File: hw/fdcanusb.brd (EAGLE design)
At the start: 45 x 32 mm, 37 parts, among them J1 MF-CON-MICROUSB-RIGHT, J3 JST-ZH6SMT_VERT, M1 MOUNT, M2 MOUNT, M3 MOUNT, M4 MOUNT, U1 MF-REG-SOT235-3.3V-300mA, U2 USBLC6-2SC6, U3 TCAN334GSOT23, U4 TLP3317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

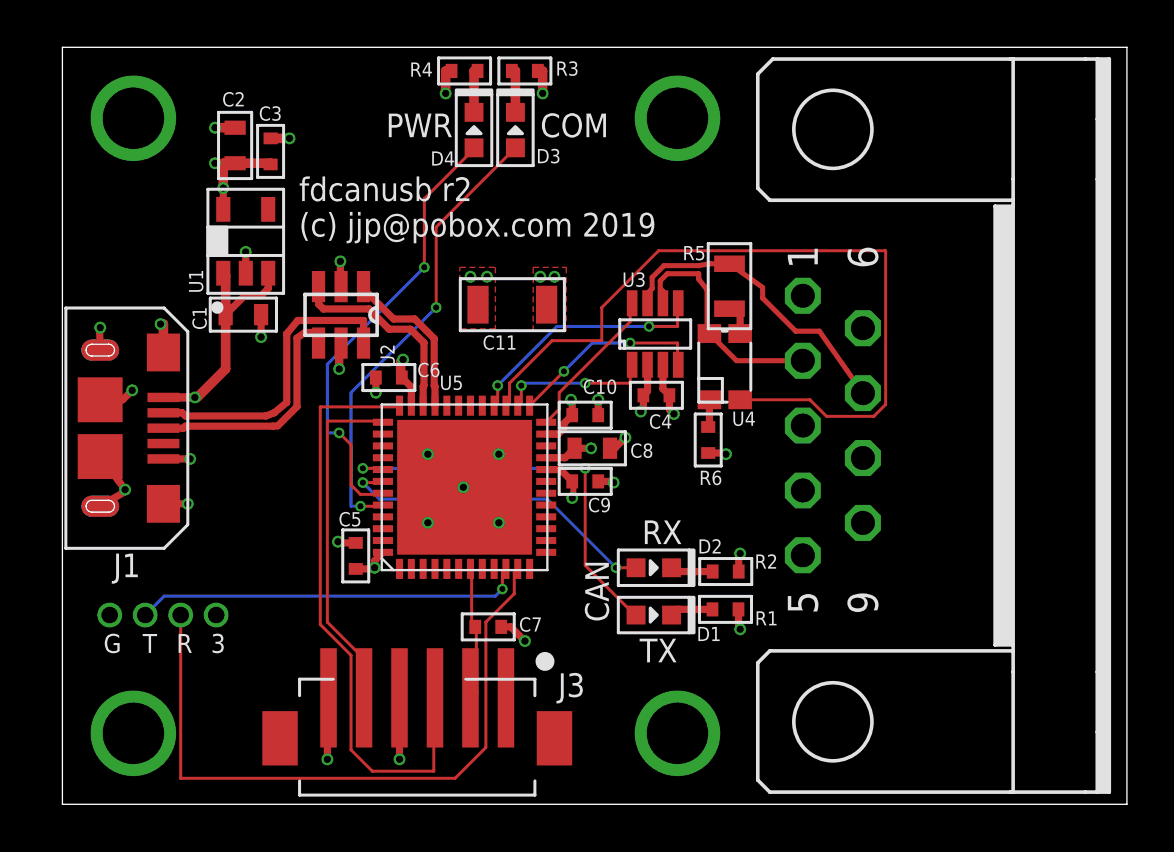
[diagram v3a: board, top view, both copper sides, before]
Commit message: Fix DB9 pinout
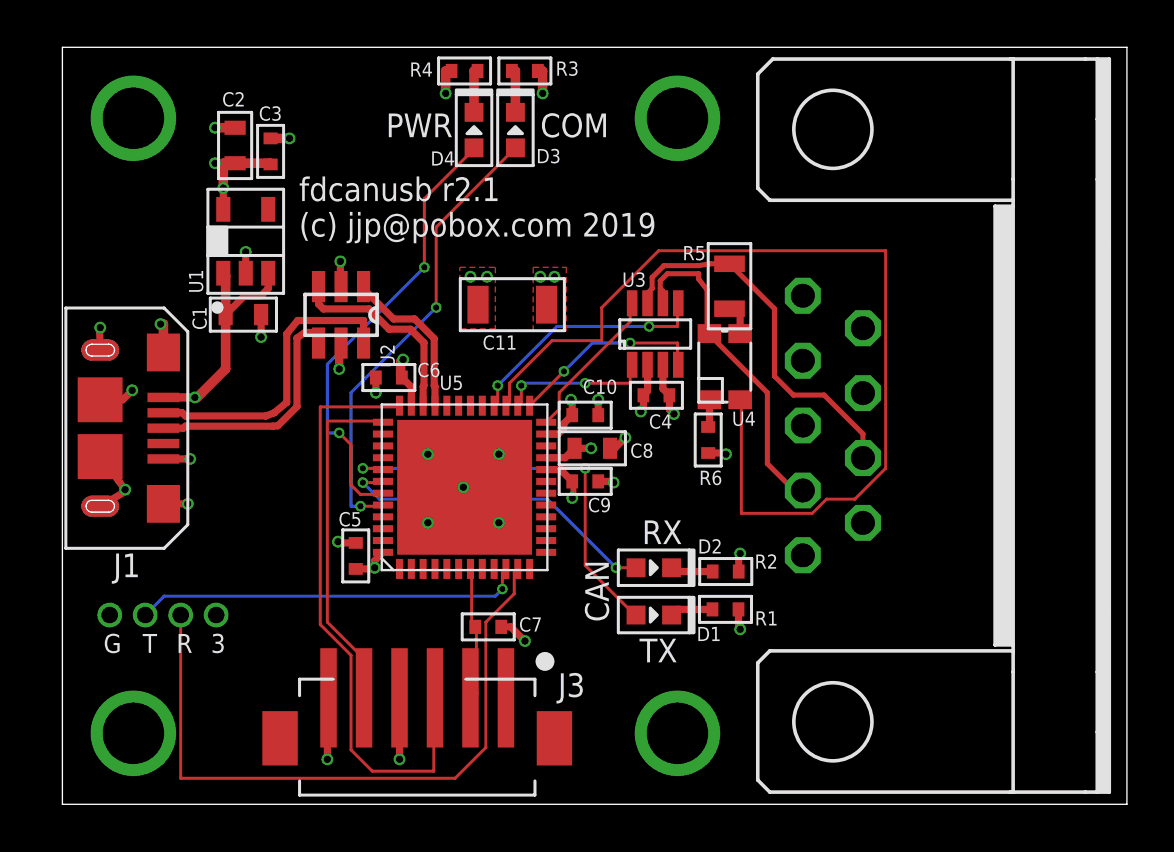
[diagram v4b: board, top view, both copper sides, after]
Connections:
- net CAN_N: now also J2.4; no longer J2.2
- net CAN_P: now also J2.8; no longer J2.7
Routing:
- net CAN_TERM: track 33.2 -> 41.0 mm
- net CAN_N: track 9.92 -> 14.0 mm
- net CAN_P: track 13.0 -> 16.0 mm
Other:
- board text added: "fdcanusb r2.1 (c) jjp@pobox.com 2019"
- board text removed: "fdcanusb r2 (c) jjp@pobox.com 2019"
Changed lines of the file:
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@@
 <wire x1="45" y1="32" x2="0" y2="32" width="0" layer="20"/>
 <wire x1="0" y1="32" x2="0" y2="0" width="0" layer="20"/>
-<text x="10" y="24" size="1" layer="21">fdcanusb r2
+<text x="10" y="24" size="1" layer="21">fdcanusb r2.1
 (c) jjp@pobox.com 2019</text>
 <text x="2.5" y="7.2" size="0.8" layer="21" rot="R180">G</text>
@@
 </signal>
 <signal name="CAN_N" class="2">
-<contactref element="J2" pad="2"/>
 <contactref element="U3" pad="6"/>
 <contactref element="U4" pad="4"/>
-<wire x1="31.3" y1="18.7532" x2="28.4968" y2="18.7532" width="0.2159" layer="1"/>
-<wire x1="28.4968" y1="18.7532" x2="27.35" y2="19.9" width="0.2159" layer="1"/>
 <wire x1="27.35" y1="19.9" x2="27.25" y2="19.9" width="0.2159" layer="1"/>
 <wire x1="27.25" y1="19.9" x2="27.25" y2="21.75" width="0.2159" layer="1"/>
@@
 <wire x1="25.27145" y1="21.8" x2="25.385" y2="21.68645" width="0.2159" layer="1"/>
 <wire x1="25.385" y1="21.68645" x2="25.385" y2="21.18" width="0.2159" layer="1"/>
+<contactref element="J2" pad="4"/>
+<wire x1="27.35" y1="19.9" x2="27.35" y2="19.85" width="0.2159" layer="1"/>
+<wire x1="27.35" y1="19.85" x2="29.8" y2="17.4" width="0.2159" layer="1"/>
+<wire x1="29.8" y1="17.4" x2="29.8" y2="14.4" width="0.2159" layer="1"/>
+<wire x1="29.8" y1="14.4" x2="30.9332" y2="13.2668" width="0.2159" layer="1"/>
+<wire x1="30.9332" y1="13.2668" x2="31.3" y2="13.2668" width="0.2159" layer="1"/>
 </signal>
 <signal name="CAN_P" class="2">
-<contactref element="J2" pad="7"/>
 <contactref element="U3" pad="7"/>
 <contactref element="R5" pad="P$1"/>
-<wire x1="33.84" y1="17.3816" x2="32" y2="20" width="0.2159" layer="1"/>
-<wire x1="32" y1="20" x2="31" y2="20" width="0.2159" layer="1"/>
-<wire x1="31" y1="20" x2="29.6" y2="21.4" width="0.2159" layer="1"/>
-<wire x1="29.6" y1="21.4" x2="29.6" y2="21.85" width="0.2159" layer="1"/>
-<wire x1="29.6" y1="21.85" x2="28.2" y2="22.85" width="0.2159" layer="1"/>
 <wire x1="28.2" y1="22.85" x2="27.37855" y2="22.85" width="0.2159" layer="1"/>
 <wire x1="27.37855" y1="22.85" x2="26.9" y2="22.77145" width="0.2159" layer="1"/>
@@
 <wire x1="24.92855" y1="21.8" x2="24.735" y2="21.60645" width="0.2159" layer="1"/>
 <wire x1="24.735" y1="21.60645" x2="24.735" y2="21.18" width="0.2159" layer="1"/>
+<contactref element="J2" pad="8"/>
+<wire x1="28.2" y1="22.85" x2="30.1" y2="20.95" width="0.2159" layer="1"/>
+<wire x1="30.1" y1="20.95" x2="30.1" y2="18.1" width="0.2159" layer="1"/>
+<wire x1="30.1" y1="18.1" x2="30.9" y2="17.3" width="0.2159" layer="1"/>
+<wire x1="30.9" y1="17.3" x2="32.2" y2="17.3" width="0.2159" layer="1"/>
+<wire x1="32.2" y1="17.3" x2="33.84" y2="15.66" width="0.2159" layer="1"/>
+<wire x1="33.84" y1="15.66" x2="33.84" y2="14.6384" width="0.2159" layer="1"/>
 </signal>
 <signal name="N$3">
@@
 <wire x1="25.2" y1="23.4" x2="22.8" y2="21" width="0.127" layer="1"/>
 <wire x1="34.8" y1="23.4" x2="25.2" y2="23.4" width="0.127" layer="1"/>
-<wire x1="34.8" y1="16.9" x2="34.8" y2="23.4" width="0.127" layer="1"/>
-<wire x1="34.3" y1="16.4" x2="34.8" y2="16.9" width="0.127" layer="1"/>
-<wire x1="32.3" y1="16.4" x2="34.3" y2="16.4" width="0.127" layer="1"/>
-<wire x1="31.6" y1="17.1" x2="32.3" y2="16.4" width="0.127" layer="1"/>
-<wire x1="28.65" y1="17.1" x2="31.6" y2="17.1" width="0.127" layer="1"/>
+<wire x1="34.8" y1="14.2" x2="34.8" y2="23.4" width="0.127" layer="1"/>
+<wire x1="33.5" y1="12.9" x2="34.8" y2="14.2" width="0.127" layer="1"/>
+<wire x1="32.3" y1="12.9" x2="33.5" y2="12.9" width="0.127" layer="1"/>
+<wire x1="31.7" y1="12.3" x2="32.3" y2="12.9" width="0.127" layer="1"/>
+<wire x1="28.7" y1="12.3" x2="31.7" y2="12.3" width="0.127" layer="1"/>
+<wire x1="28.7" y1="17.1" x2="28.7" y2="12.3" width="0.127" layer="1"/>
+<wire x1="28.7" y1="17.1" x2="28.65" y2="17.1" width="0.127" layer="1"/>
 </signal>
 <signal name="N$8">

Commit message: Update to r2.2
This just reduces the size of the PCB so it doesn't hang out so far
under the DB-9 connector.
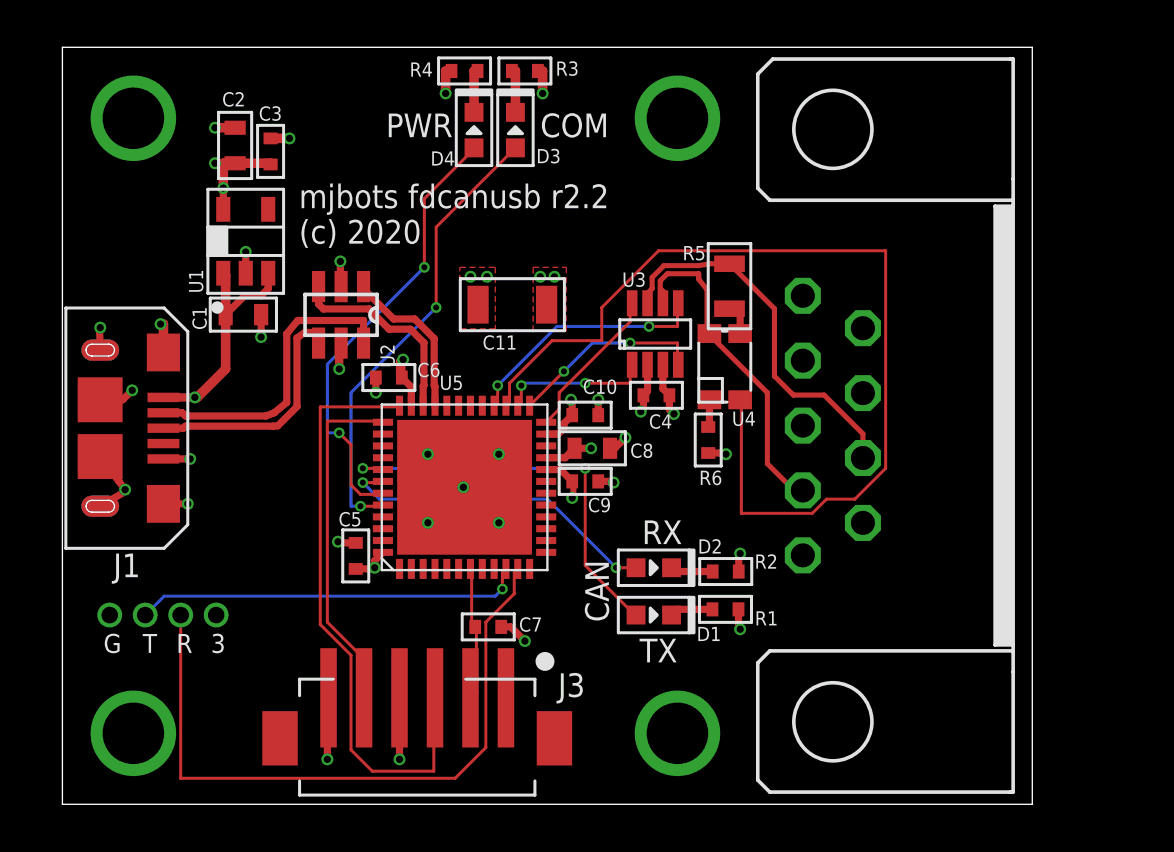
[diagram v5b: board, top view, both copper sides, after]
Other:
- board size 45 x 32 mm -> 41 x 32 mm
- board text added: "mjbots fdcanusb r2.2 (c) 2020"
- board text removed: "fdcanusb r2.1 (c) jjp@pobox.com 2019"
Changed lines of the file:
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@@
 <board>
 <plain>
-<wire x1="0" y1="0" x2="45" y2="0" width="0" layer="20"/>
-<wire x1="45" y1="0" x2="45" y2="32" width="0" layer="20"/>
-<wire x1="45" y1="32" x2="0" y2="32" width="0" layer="20"/>
+<wire x1="0" y1="0" x2="41" y2="0" width="0" layer="20"/>
+<wire x1="41" y1="0" x2="41" y2="32" width="0" layer="20"/>
+<wire x1="41" y1="32" x2="0" y2="32" width="0" layer="20"/>
 <wire x1="0" y1="32" x2="0" y2="0" width="0" layer="20"/>
-<text x="10" y="24" size="1" layer="21">fdcanusb r2.1
-(c) jjp@pobox.com 2019</text>
+<text x="10" y="23.7" size="1" layer="21">mjbots fdcanusb r2.2
+(c) 2020</text>
 <text x="2.5" y="7.2" size="0.8" layer="21" rot="R180">G</text>
 <text x="6.9" y="7.2" size="0.8" layer="21" rot="R180">3</text>
@@
 <polygon width="0.254" layer="2" thermals="no">
 <vertex x="0.5" y="31.5"/>
-<vertex x="44.5" y="31.5"/>
-<vertex x="44.5" y="0.5"/>
+<vertex x="40.5" y="31.5"/>
+<vertex x="40.5" y="0.5"/>
 <vertex x="0.5" y="0.5"/>
 </polygon>
@@
 <polygon width="0.254" layer="15" thermals="no">
 <vertex x="0.5" y="31.5"/>
-<vertex x="44.5" y="31.5"/>
-<vertex x="44.5" y="0.5"/>
+<vertex x="40.5" y="31.5"/>
+<vertex x="40.5" y="0.5"/>
 <vertex x="0.5" y="0.5"/>
 </polygon>

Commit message: Switch LED resistors back to 220s
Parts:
- R1, R2, R3, R4: value 560 -> 220
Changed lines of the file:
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@@
 <attribute name="NAME" x="16.6" y="27.6" size="0.6" layer="25" font="vector" ratio="10" rot="R180"/>
 </element>
-<element name="R1" library="mfpassives" package="R0402" value="560" x="28.03" y="8.24" smashed="yes" rot="R180">
+<element name="R1" library="mfpassives" package="R0402" value="220" x="28.03" y="8.24" smashed="yes" rot="R180">
 <attribute name="HOUSEPART" value="" x="-21.5" y="69.2" size="1.778" layer="27" rot="R180" display="off"/>
 <attribute name="TOLERANCE" value="" x="-21.5" y="69.2" size="1.778" layer="27" rot="R180" display="off"/>
-<attribute name="MPN" value="MF-RES-0402-560" x="-21.5" y="69.2" size="1.778" layer="27" rot="R180" display="off"/>
+<attribute name="MPN" value="MF-RES-0402-220" x="-21.5" y="69.2" size="1.778" layer="27" rot="R180" display="off"/>
 <attribute name="POPULATE" value="1" x="-21.5" y="69.2" size="1.778" layer="27" rot="R180" display="off"/>
 <attribute name="VOLTAGE" value="" x="-21.5" y="69.2" size="1.778" layer="27" rot="R180" display="off"/>
@@
 <attribute name="NAME" x="29.27" y="7.56" size="0.6" layer="25" font="vector" ratio="10"/>
 </element>
-<element name="R2" library="mfpassives" package="R0402" value="560" x="28.04" y="9.84" smashed="yes" rot="R180">
+<element name="R2" library="mfpassives" package="R0402" value="220" x="28.04" y="9.84" smashed="yes" rot="R180">
 <attribute name="HOUSEPART" value="" x="-25.3" y="70.8" size="1.778" layer="27" rot="R180" display="off"/>
 <attribute name="TOLERANCE" value="" x="-25.3" y="70.8" size="1.778" layer="27" rot="R180" display="off"/>
-<attribute name="MPN" value="MF-RES-0402-560" x="-25.3" y="70.8" size="1.778" layer="27" rot="R180" display="off"/>
+<attribute name="MPN" value="MF-RES-0402-220" x="-25.3" y="70.8" size="1.778" layer="27" rot="R180" display="off"/>
 <attribute name="POPULATE" value="1" x="-25.3" y="70.8" size="1.778" layer="27" rot="R180" display="off"/>
 <attribute name="VOLTAGE" value="" x="-25.3" y="70.8" size="1.778" layer="27" rot="R180" display="off"/>
@@
 <attribute name="NAME" x="29.26" y="9.96" size="0.6" layer="25" font="vector" ratio="10"/>
 </element>
-<element name="R3" library="mfpassives" package="R0402" value="560" x="19.55" y="31" smashed="yes" rot="R180">
+<element name="R3" library="mfpassives" package="R0402" value="220" x="19.55" y="31" smashed="yes" rot="R180">
 <attribute name="HOUSEPART" value="" x="5.58" y="95.77" size="1.778" layer="27" rot="R180" display="off"/>
 <attribute name="TOLERANCE" value="" x="5.58" y="95.77" size="1.778" layer="27" rot="R180" display="off"/>
-<attribute name="MPN" value="MF-RES-0402-560" x="5.58" y="95.77" size="1.778" layer="27" rot="R180" display="off"/>
+<attribute name="MPN" value="MF-RES-0402-220" x="5.58" y="95.77" size="1.778" layer="27" rot="R180" display="off"/>
 <attribute name="POPULATE" value="1" x="5.58" y="95.77" size="1.778" layer="27" rot="R180" display="off"/>
 <attribute name="VOLTAGE" value="" x="5.58" y="95.77" size="1.778" layer="27" rot="R180" display="off"/>
@@
 <attribute name="NAME" x="20.85" y="30.8" size="0.6" layer="25" font="vector" ratio="10"/>
 </element>
-<element name="R4" library="mfpassives" package="R0402" value="560" x="17" y="31" smashed="yes">
+<element name="R4" library="mfpassives" package="R0402" value="220" x="17" y="31" smashed="yes">
 <attribute name="HOUSEPART" value="" x="34.78" y="-33.77" size="1.778" layer="27" display="off"/>
 <attribute name="TOLERANCE" value="" x="34.78" y="-33.77" size="1.778" layer="27" display="off"/>
-<attribute name="MPN" value="MF-RES-0402-560" x="34.78" y="-33.77" size="1.778" layer="27" display="off"/>
+<attribute name="MPN" value="MF-RES-0402-220" x="34.78" y="-33.77" size="1.778" layer="27" display="off"/>
 <attribute name="POPULATE" value="1" x="34.78" y="-33.77" size="1.778" layer="27" display="off"/>
 <attribute name="VOLTAGE" value="" x="34.78" y="-33.77" size="1.778" layer="27" display="off"/>

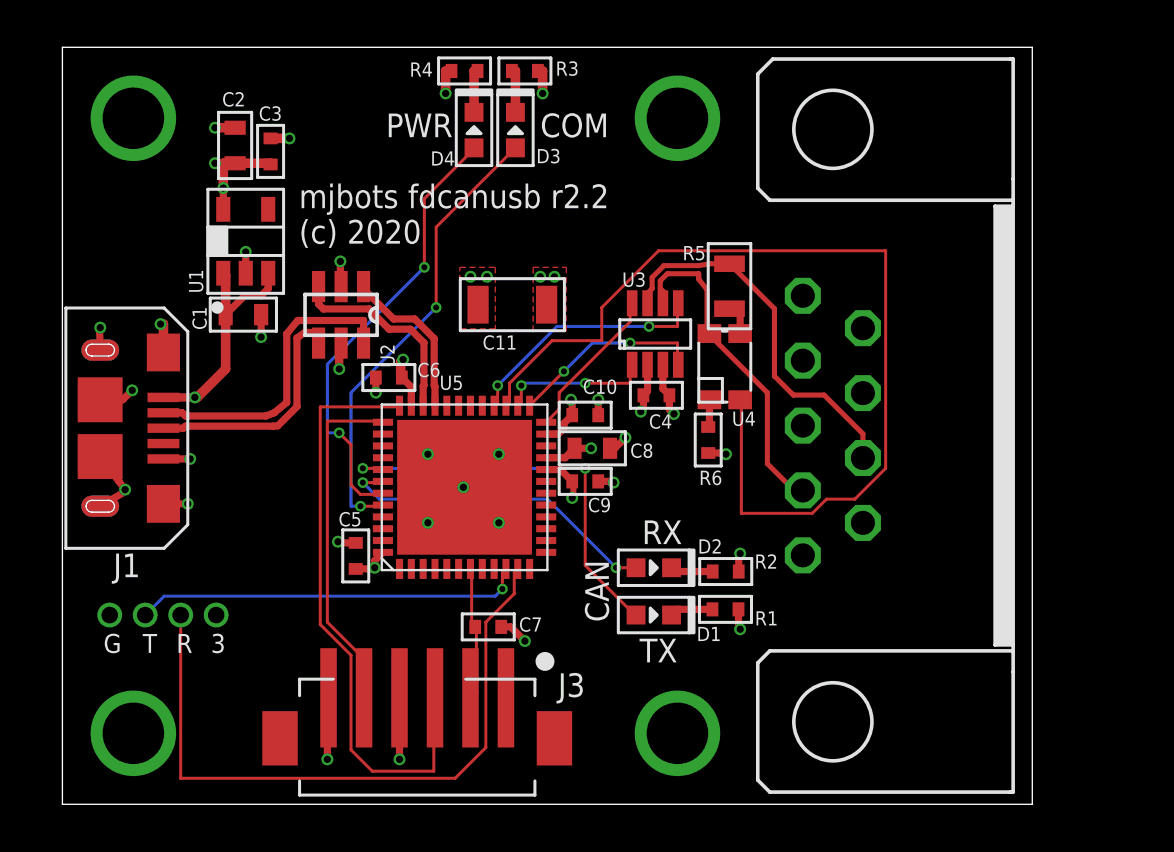
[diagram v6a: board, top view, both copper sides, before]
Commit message: Make DB9 have plated holes for retaining clips
This should improve the mechanical strength of the DB9 connector when
installed
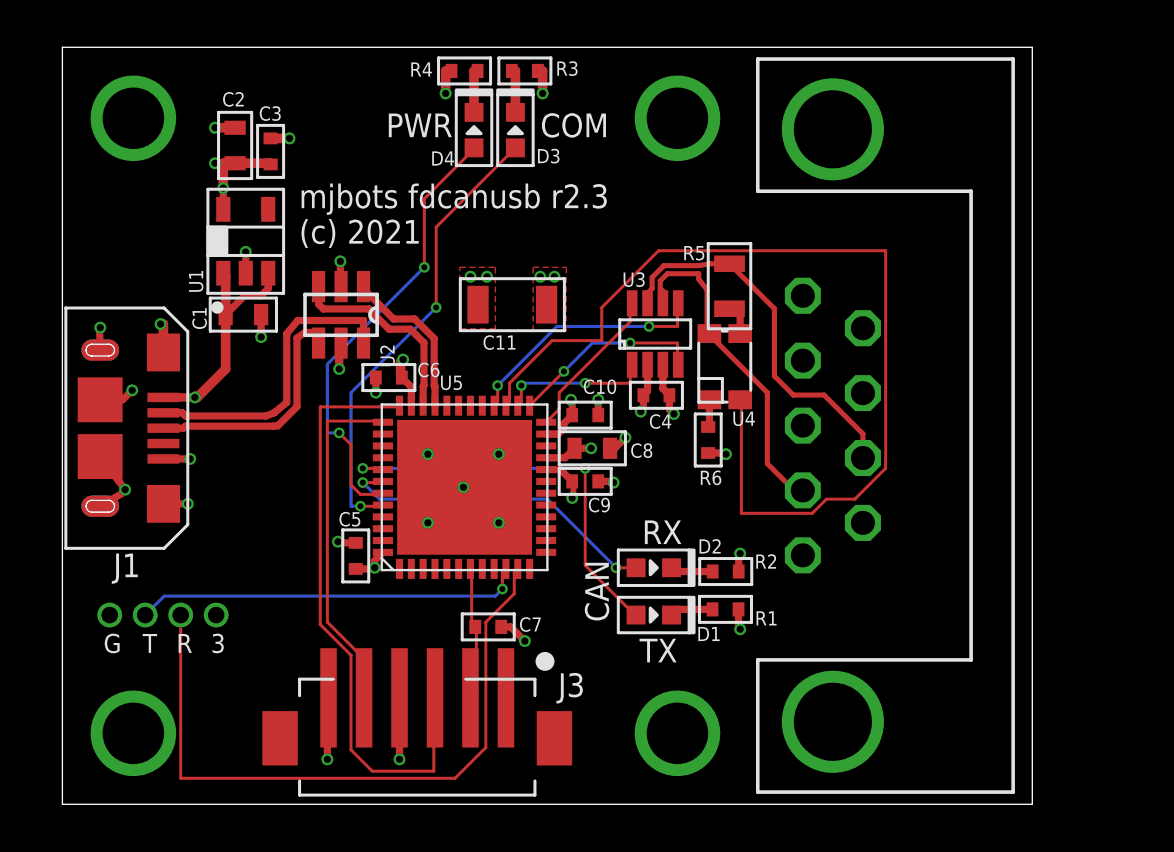
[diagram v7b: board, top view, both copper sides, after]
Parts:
- J2: device fdcanusb:F09H -> fdcanusb:DB09_PLATED
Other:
- board text added: "mjbots fdcanusb r2.3 (c) 2021"
- board text removed: "mjbots fdcanusb r2.2 (c) 2020"
